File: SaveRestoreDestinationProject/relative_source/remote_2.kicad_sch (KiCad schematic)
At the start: 3 parts

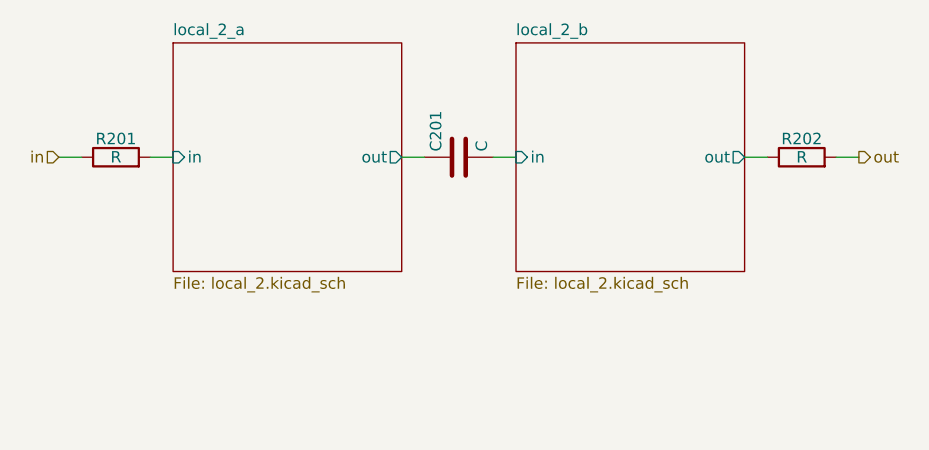
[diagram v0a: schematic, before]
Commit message: Add support for connected drawings, update test template
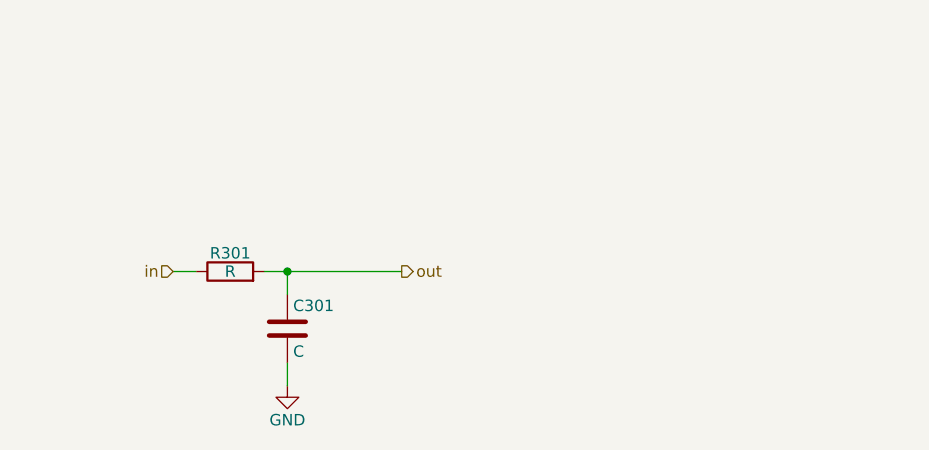
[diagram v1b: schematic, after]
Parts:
- removed C201: C, Capacitor_SMD:C_1206_3216Metric, symbol Device:C
- removed R201, R202: R, Resistor_SMD:R_1206_3216Metric, symbol Device:R
- added C301: C, Capacitor_SMD:C_1206_3216Metric, symbol Device:C
- added R301: R, Resistor_SMD:R_1206_3216Metric, symbol Device:R
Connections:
- net in: now also R301.1
- net out: now also C301.1, R301.2
- new net GND: C301.2
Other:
- removed sheet local_2_a
- removed sheet local_2_b
